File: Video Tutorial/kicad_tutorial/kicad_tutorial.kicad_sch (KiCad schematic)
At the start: 5 parts, among them SW1 SW_SPDT, U1 STM32F405RGT6

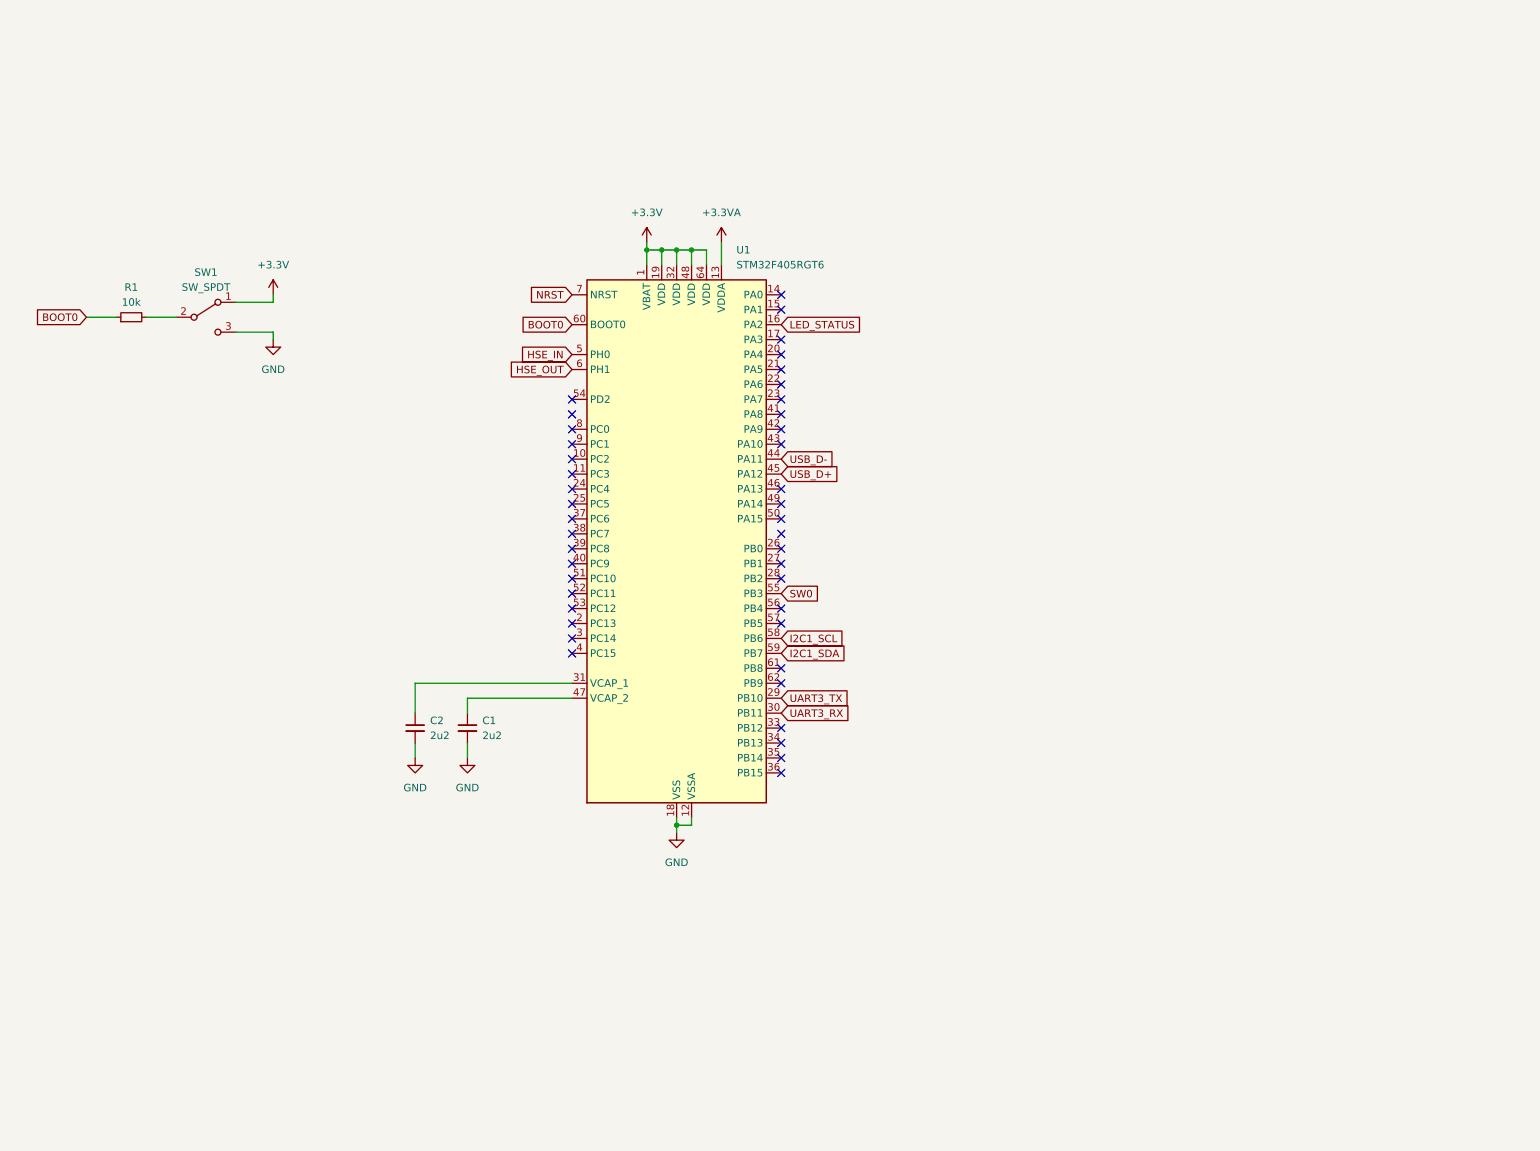
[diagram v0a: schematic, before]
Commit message: Added notes for Chapter: Buck converter circuitry
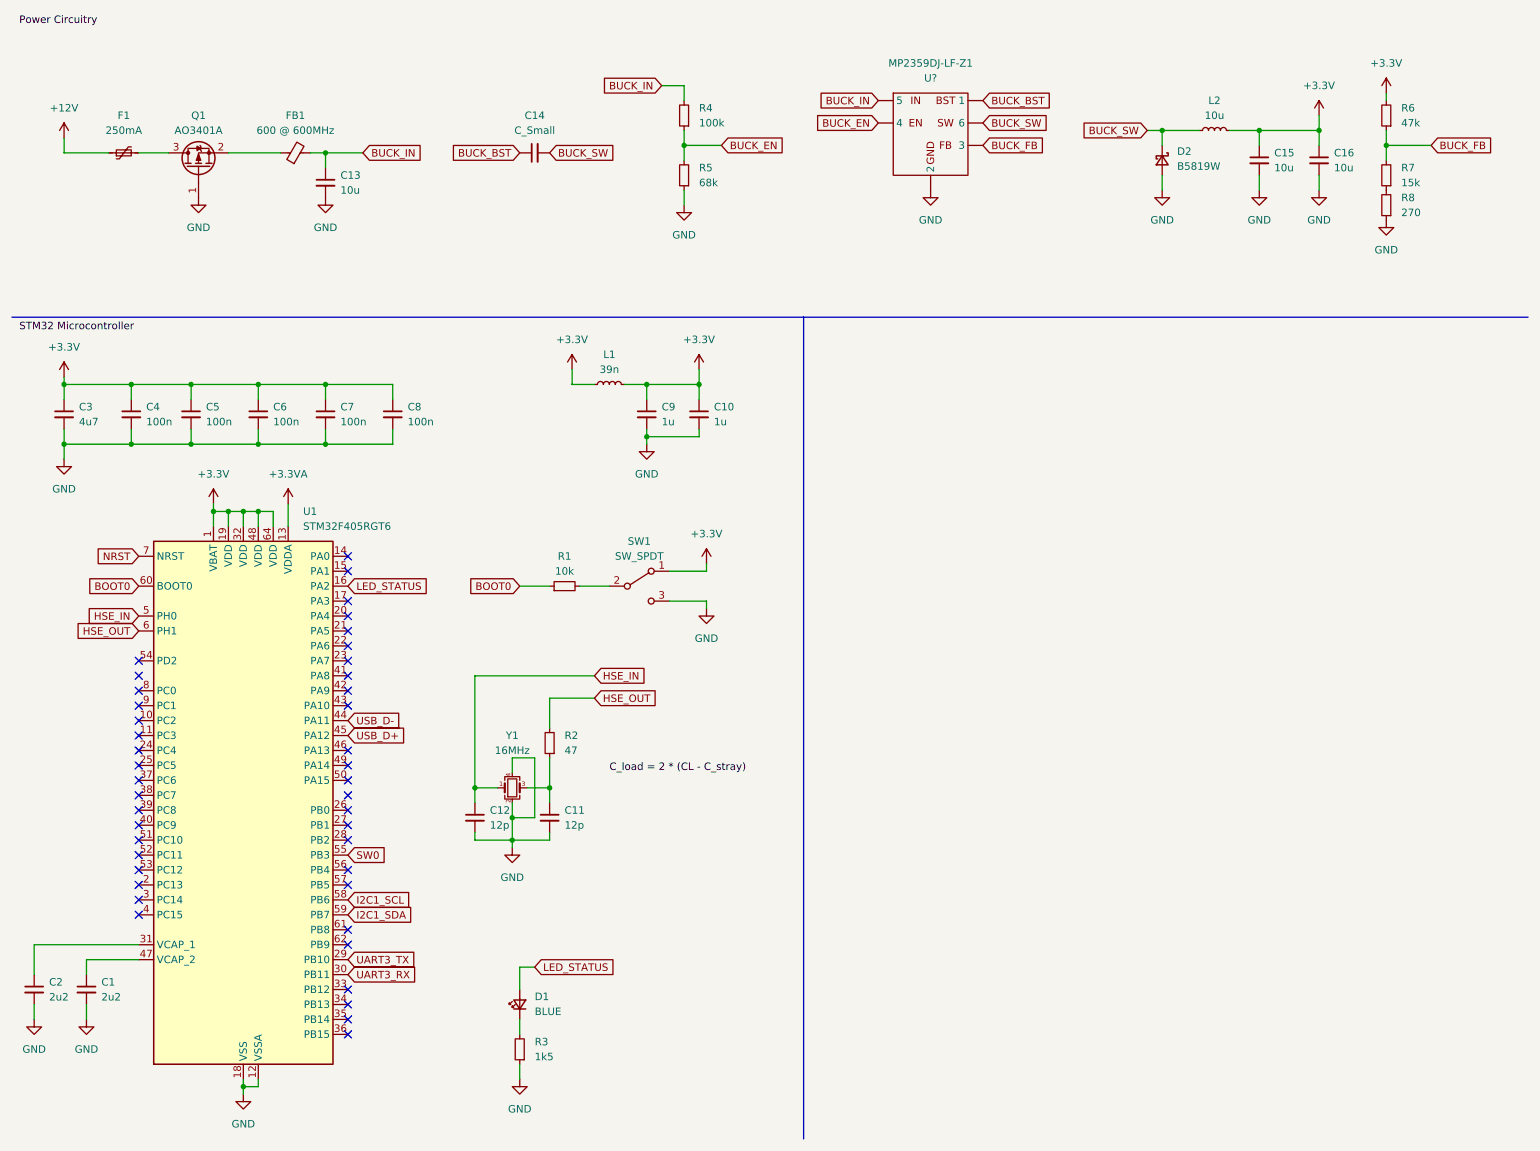
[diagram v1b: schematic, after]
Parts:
- added C10, C9: 1u, symbol Device:C_Small
- added C11, C12: 12p, symbol Device:C_Small
- added C13, C15, C16: 10u, symbol Device:C_Small
- added C14: C_Small, symbol Device:C_Small
- added C3: 4u7, symbol Device:C_Small
- added C4, C5, C6, C7, C8: 100n, symbol Device:C_Small
- added D1: BLUE, symbol Device:LED_Small
- added D2: B5819W, symbol Device:D_Schottky_Small
- added F1: 250mA, symbol Device:Polyfuse_Small
- added FB1: 600 @ 600MHz, symbol Device:FerriteBead_Small
- added L1: 39n, symbol Device:L_Small
- added L2: 10u, symbol Device:L_Small
- added MP2359DJ-LF-Z1: U?, symbol Custom:MP2359DJ-LF-Z
- added Q1: AO3401A, Package_TO_SOT_SMD:SOT-23, symbol Transistor_FET:AO3401A
- added R2: 47, symbol Device:R_Small
- added R3: 1k5, symbol Device:R_Small
- added R4: 100k, symbol Device:R_Small
- added R5: 68k, symbol Device:R_Small
- added R6: 47k, symbol Device:R_Small
- added R7: 15k, symbol Device:R_Small
- added R8: 270, symbol Device:R_Small
- added Y1: 16MHz, symbol Device:Crystal_GND24_Small
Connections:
- net +3.3V: now also C10.1, C15.1, C16.1, C3.1, C4.1, C5.1, C6.1, C7.1, C8.1, C9.1, L1.1, L1.2, L2.2, R6.2
- net GND: now also C10.2, C11.2, C12.2, C13.2, C15.2, C16.2, C3.2, C4.2, C5.2, C6.2, C7.2, C8.2, C9.2, D2.2 (A), MP2359DJ-LF-Z1. (6), Q1.1 (G), R3.1, R5.1, R8.1, Y1.2, Y1.4
- net HSE_IN: now also C12.1, Y1.1
- net HSE_OUT: now also R2.2
- net LED_STATUS: now also D1.2 (A)
- new net: C11.1, R2.1, Y1.3
- new net: FB1.1, Q1.2 (S)
- new net: F1.2, Q1.3 (D)
- new net: R7.1, R8.2
- new net: D1.1 (K), R3.2
- new net +12V: F1.1
- new net BUCK_BST: C14.1, MP2359DJ-LF-Z1. (6)
- new net BUCK_EN: MP2359DJ-LF-Z1. (6), R4.1, R5.2
- new net BUCK_FB: MP2359DJ-LF-Z1. (6), R6.1, R7.2
- new net BUCK_IN: C13.1, FB1.2, MP2359DJ-LF-Z1. (6), R4.2
- new net BUCK_SW: C14.2, D2.1 (K), L2.1, MP2359DJ-LF-Z1. (6)
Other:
- moved on the sheet: C1, C2, R1, SW1, U1

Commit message: Added notes for Chapter: USB
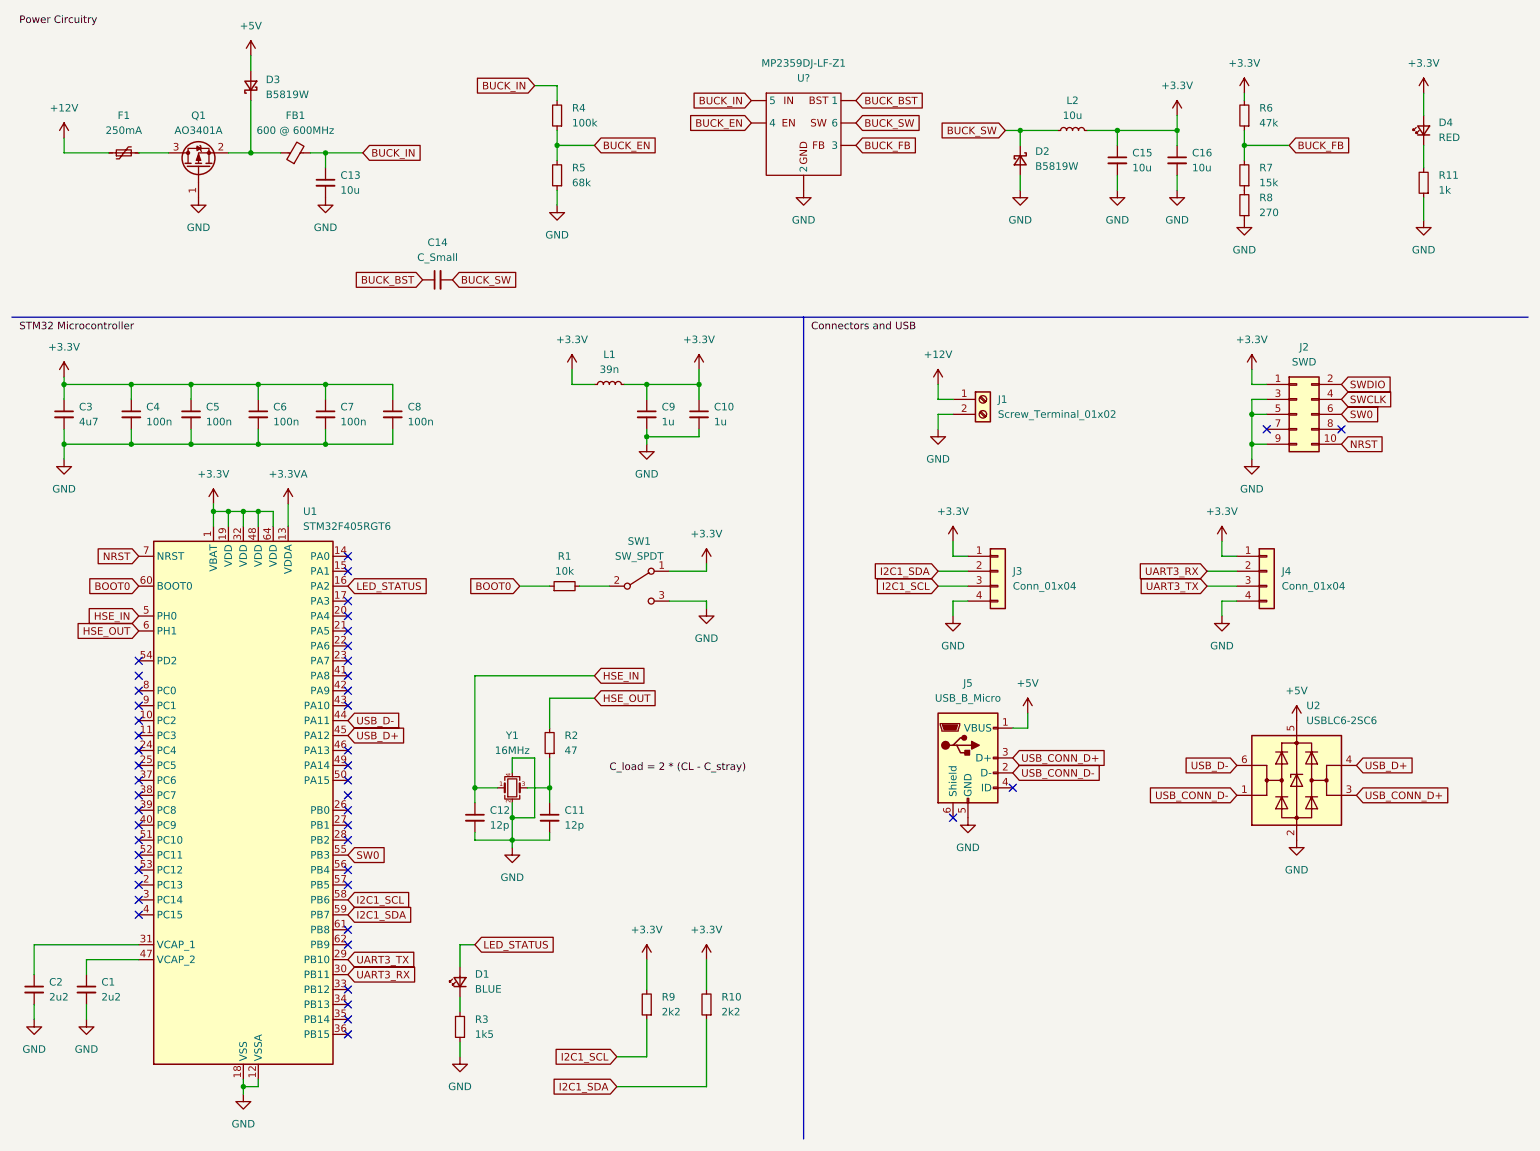
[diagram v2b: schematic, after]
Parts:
- added D3: B5819W, symbol Device:D_Schottky_Small
- added D4: RED, symbol Device:LED_Small
- added J1: Screw_Terminal_01x02, symbol Connector:Screw_Terminal_01x02
- added J2: SWD, symbol Connector_Generic:Conn_02x05_Odd_Even
- added J3, J4: Conn_01x04, symbol Connector_Generic:Conn_01x04
- added J5: USB_B_Micro, symbol Connector:USB_B_Micro
- added R10, R9: 2k2, symbol Device:R_Small
- added R11: 1k, symbol Device:R_Small
- added U2: USBLC6-2SC6, Package_TO_SOT_SMD:SOT-23-6, symbol Power_Protection:USBLC6-2SC6
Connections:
- net +12V: now also J1.1 (Pin_1)
- net +3.3V: now also D4.2 (A), J2.1 (Pin_1), J3.1 (Pin_1), J4.1 (Pin_1), R10.2, R9.2
- net GND: now also J1.2 (Pin_2), J2.3 (Pin_3), J2.5 (Pin_5), J2.9 (Pin_9), J3.4 (Pin_4), J4.4 (Pin_4), J5.5 (GND), R11.1, U2.2 (GND)
- net I2C1_SCL: now also J3.3 (Pin_3), R9.1
- net I2C1_SDA: now also J3.2 (Pin_2), R10.1
- net NRST: now also J2.10 (Pin_10)
- net SW0: now also J2.6 (Pin_6)
- net UART3_RX: now also J4.2 (Pin_2)
- net UART3_TX: now also J4.3 (Pin_3)
- net USB_D+: now also U2.4 (I/O2)
- net USB_D-: now also U2.6 (I/O1)
- net at FB1.1, Q1.2 (S): now also D3.1 (K)
- new net: D4.1 (K), R11.2
- new net +5V: D3.2 (A), J5.1 (VBUS), U2.5 (VBUS)
- new net SWCLK: J2.4 (Pin_4)
- new net SWDIO: J2.2 (Pin_2)
- new net USB_CONN_D+: J5.3 (D+), U2.3 (I/O2)
- new net USB_CONN_D-: J5.2 (D-), U2.1 (I/O1)
- no-connect marks 43 -> 47
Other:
- moved on the sheet: C14, C15, C16, D1, D2, L2, MP2359DJ-LF-Z1, R3, R4, R5, R6, R7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

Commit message: Added notes for Chapter: Design Rules
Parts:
- added H1, H2, H3, H4: MountingHole_Pad, MountingHole:MountingHole_4.3mm_M4_Pad_Via, symbol Mechanical:MountingHole_Pad
- C1, C2, C3: footprint (none) -> Capacitor_SMD:C_0603_1608Metric
- C10, C11, C12, C4, C5, C6, C7, C8, C9: footprint (none) -> Capacitor_SMD:C_0402_1005Metric
- C13, C15, C16: footprint (none) -> Capacitor_SMD:C_1206_3216Metric
- C14: value C_Small -> 10n; footprint (none) -> Capacitor_SMD:C_0603_1608Metric
- D1, D4: footprint (none) -> LED_SMD:LED_0603_1608Metric
- D2, D3: footprint (none) -> Diode_SMD:D_SOD-123
- F1: footprint (none) -> Fuse:Fuse_1206_3216Metric
- FB1: footprint (none) -> Inductor_SMD:L_0805_2012Metric
- J1: footprint (none) -> TerminalBlock_Phoenix:TerminalBlock_Phoenix_PT-1,5-2-3.5-H_1x02_P3.50mm_Horizontal
- J2: footprint (none) -> Connector_PinHeader_1.27mm:PinHeader_2x05_P1.27mm_Vertical_SMD
- J3, J4: footprint (none) -> Connector_Molex:Molex_PicoBlade_53048-0410_1x04_P1.25mm_Horizontal
- J5: footprint (none) -> Connector_USB:USB_Micro-B_GCT_USB3076-30-A
- L1: footprint (none) -> Inductor_SMD:L_0402_1005Metric
- L2: footprint (none) -> Inductor_SMD:L_Sunlord_MWSA0518S
- R1, R10, R2, R9: footprint (none) -> Resistor_SMD:R_0402_1005Metric
- R11, R3, R4, R5, R6, R7, R8: footprint (none) -> Resistor_SMD:R_0603_1608Metric
- SW1: footprint (none) -> Button_Switch_SMD:SW_SPDT_PCM12
- U1: renamed from MP2359DJ-LF-Z1; value U? -> MP2359DJ-LF-Z; footprint (none) -> Package_TO_SOT_SMD:SOT-23-6
- Y1: footprint (none) -> Crystal:Crystal_SMD_3225-4Pin_3.2x2.5mm
- renumbered U1 to U2, U2 to U3
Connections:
- net GND: now also H1.1, H2.1, H3.1, H4.1
- net SWCLK: now also U2.49 (PA14)
- net SWDIO: now also U2.46 (PA13)
- no-connect marks 47 -> 43
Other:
- moved on the sheet: J4

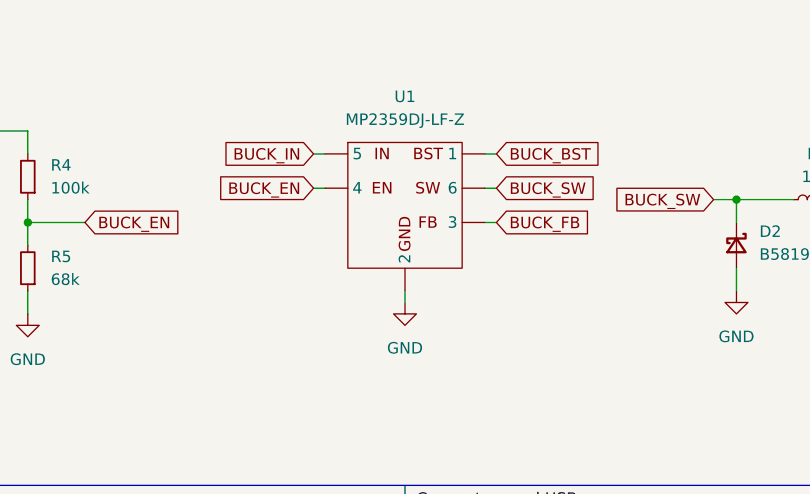
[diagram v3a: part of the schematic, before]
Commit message: Added notes for Chapter: Rough layout, finer details
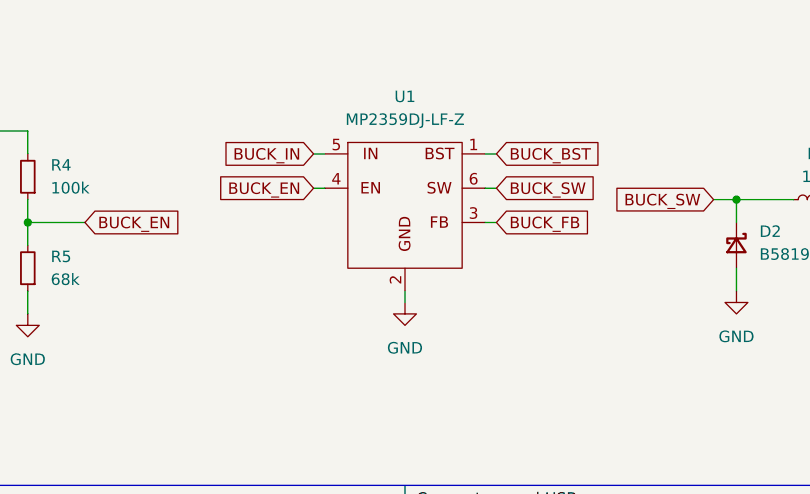
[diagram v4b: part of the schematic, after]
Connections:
- net BUCK_BST: now also U1.1; no longer U1. (6)
- net BUCK_EN: now also U1.4; no longer U1. (6)
- net BUCK_FB: now also U1.3; no longer U1. (6)
- net BUCK_IN: now also U1.5; no longer U1. (6)
- net BUCK_SW: now also U1.6; no longer U1. (6)
- net GND: now also U1.2; no longer U1. (6)
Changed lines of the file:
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@@
-    )
-  )
-  (symbol (lib_id "Custom:MP2359DJ-LF-Z") (at 146.05 33.02 0) (unit 1)
-    (in_bom yes) (on_board yes) (dnp no) (fields_autoplaced)
-    (property "Reference" "U1" (at 146.05 21.59 0)
-      (effects (font (size 1.27 1.27)))
-    )
-    (property "Value" "MP2359DJ-LF-Z" (at 146.05 24.13 0)
-      (effects (font (size 1.27 1.27)))
-    )
-    (property "Footprint" "Package_TO_SOT_SMD:SOT-23-6" (at 146.05 21.59 0)
-      (effects (font (size 1.27 1.27)) hide)
-    )
-    (property "Datasheet" "" (at 146.05 21.59 0)
-      (effects (font (size 1.27 1.27)) hide)
-    )
-    (pin "")
-    (pin "")
-    (pin "")
-    (pin "")
-    (pin "")
-    (pin "")
-    (instances
-      (project "kicad_tutorial"
-        (path "/6ff00282-45b6-4130-8daf-dd7fa29b8a4f"
-          (reference "U1") (unit 1)
-        )
-      )
     )
   )
@@
         )
       )
+    )
+  )
+  (symbol (lib_id "Custom:MP2359DJ-LF-Z") (at 146.05 33.02 0) (unit 1)
+    (in_bom yes) (on_board yes) (dnp no) (fields_autoplaced)
+    (property "Reference" "U1" (at 146.05 21.59 0)
+      (effects (font (size 1.27 1.27)))
+    )
+    (property "Value" "MP2359DJ-LF-Z" (at 146.05 24.13 0)
+      (effects (font (size 1.27 1.27)))
+    )
+    (property "Footprint" "Package_TO_SOT_SMD:SOT-23-6" (at 146.05 21.59 0)
+      (effects (font (size 1.27 1.27)) hide)
+    )
+    (property "Datasheet" "" (at 146.05 21.59 0)
+      (effects (font (size 1.27 1.27)) hide)
+    )
+    (pin "1")
+    (pin "2")
+    (pin "3")
+    (pin "4")
+    (pin "5")
+    (pin "6")
+    (instances
+      (project "kicad_tutorial"
+        (path "/6ff00282-45b6-4130-8daf-dd7fa29b8a4f"
+          (reference "U1") (unit 1)
+        )
+      )
